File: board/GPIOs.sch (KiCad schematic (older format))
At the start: 3 parts

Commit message: Issue #1481 - GPIO sheet
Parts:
- gave numbers to parts that had none: 3
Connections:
- net labels added: DIFFCLK_A0N, DIFFCLK_A0P, DIFFCLK_A1N, DIFFCLK_A1P, DIFFCLK_B0N, DIFFCLK_B0P, DIFFCLK_B1N, DIFFCLK_B1P, DIFFCLK_XN, DIFFCLK_XP, DIFFIO_A0N, DIFFIO_A0P, DIFFIO_A1N, DIFFIO_A1P, DIFFIO_A2N, DIFFIO_A2P, DIFFIO_A3N, DIFFIO_A3P, DIFFIO_A4N, DIFFIO_A4P, DIFFIO_A5N, DIFFIO_A5P, DIFFIO_A6N, DIFFIO_A6P, DIFFIO_B0P, DIFFIO_B1N, DIFFIO_B1P, DIFFIO_B2N, DIFFIO_B2P, DIFFIO_B3N, DIFFIO_B3P, DIFFIO_B4N, DIFFIO_B4P, DIFFIO_B5N, DIFFIO_B5P, DIFFIO_B6N, DIFFIO_B6P, DIFFIO_XN, DIFFIO_XP, DIFFIO_YN, DIFFIO_YP, DIFFIO_ZN, DIFFIO_ZP, GPIO0, GPIO1, GPIO10, GPIO11, GPIO12, GPIO13, GPIO14, GPIO15, GPIO2, GPIO3, GPIO4, GPIO5, GPIO6, GPIO7, GPIO8, GPIO9, GPIO[0..15], PCIE_RESET, SMCLK, SMDATA, VCC3V3, ~RST
- net labels removed: GPIOA0, GPIOA1, GPIOA10, GPIOA11, GPIOA12, GPIOA13, GPIOA14, GPIOA15, GPIOA16, GPIOA17, GPIOA18, GPIOA19, GPIOA2, GPIOA20, GPIOA21, GPIOA22, GPIOA23, GPIOA24, GPIOA25, GPIOA26, GPIOA27, GPIOA28, GPIOA29, GPIOA3, GPIOA30, GPIOA31, GPIOA32, GPIOA33, GPIOA34, GPIOA35, GPIOA36, GPIOA37, GPIOA38, GPIOA39, GPIOA4, GPIOA40, GPIOA41, GPIOA42, GPIOA43, GPIOA44, GPIOA45, GPIOA46, GPIOA47, GPIOA48, GPIOA49, GPIOA5, GPIOA50, GPIOA51, GPIOA52, GPIOA53, GPIOA54, GPIOA6, GPIOA7, GPIOA8, GPIOA9, GPIOB0, GPIOB1, GPIOB10, GPIOB11, GPIOB12, GPIOB13, GPIOB14, GPIOB15, GPIOB16, GPIOB17, GPIOB18, GPIOB19, GPIOB2, GPIOB20, GPIOB21, GPIOB22, GPIOB23, GPIOB24, GPIOB25, GPIOB26, GPIOB27, GPIOB28, GPIOB29, GPIOB3, GPIOB30, GPIOB31, GPIOB32, GPIOB33, GPIOB34, GPIOB35, GPIOB36, GPIOB37, GPIOB38, GPIOB39, GPIOB4, GPIOB40, GPIOB41, GPIOB42, GPIOB43, GPIOB44, GPIOB45, GPIOB46, GPIOB47, GPIOB48, GPIOB49, GPIOB5, GPIOB50, GPIOB51, GPIOB52, GPIOB53, GPIOB6, GPIOB7, GPIOB8, GPIOB9
- wire segments 102 -> 131
- no-connect marks 5 -> 0

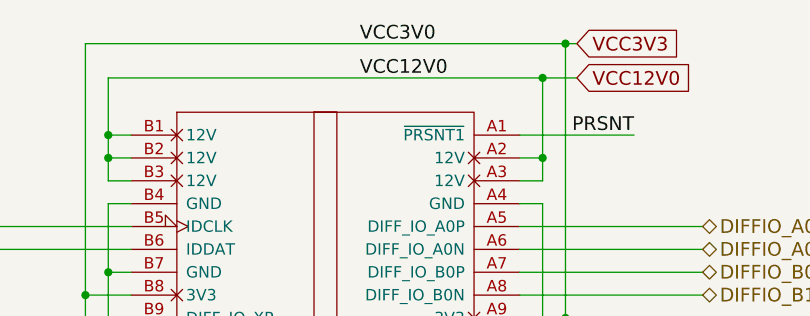
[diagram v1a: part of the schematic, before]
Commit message: Issue #1481 - CYPRESS-FPGA CONNECTIONS ADDED
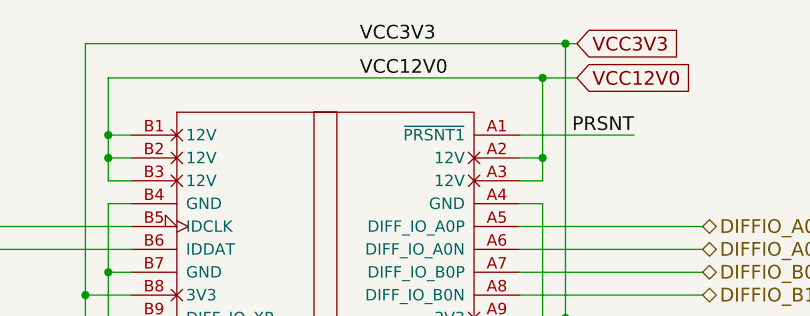
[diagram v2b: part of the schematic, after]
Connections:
- net VCC3V3: no longer P14.11, P14.12, P15.11, P15.12
- new net VCC3V0: P14.11, P14.12, P15.11, P15.12
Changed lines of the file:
@@
 $Descr A4 11693 8268
 encoding utf-8
-Sheet 12 12
+Sheet 10 12
 Title "HDMI2USB"
-Date "20 feb 2015"
+Date "24 feb 2015"
 Rev "Rev2"
 Comp ""
@@
 $EndComp
 $Comp
-L GND #PWR46
+L GND #PWR042
 U 1 1 54E50EB2
 P 4500 7200
-F 0 "#PWR46" H 4500 7200 30  0001 C CNN
+F 0 "#PWR042" H 4500 7200 30  0001 C CNN
 F 1 "GND" H 4500 7130 30  0001 C CNN
 F 2 "" H 4500 7200 60  0000 C CNN
@@
 VCC12V0
 Text Label 4650 1050 0    60   ~ 0
-VCC3V0
+VCC3V3
 $Comp
 L CONN_6X2 P14

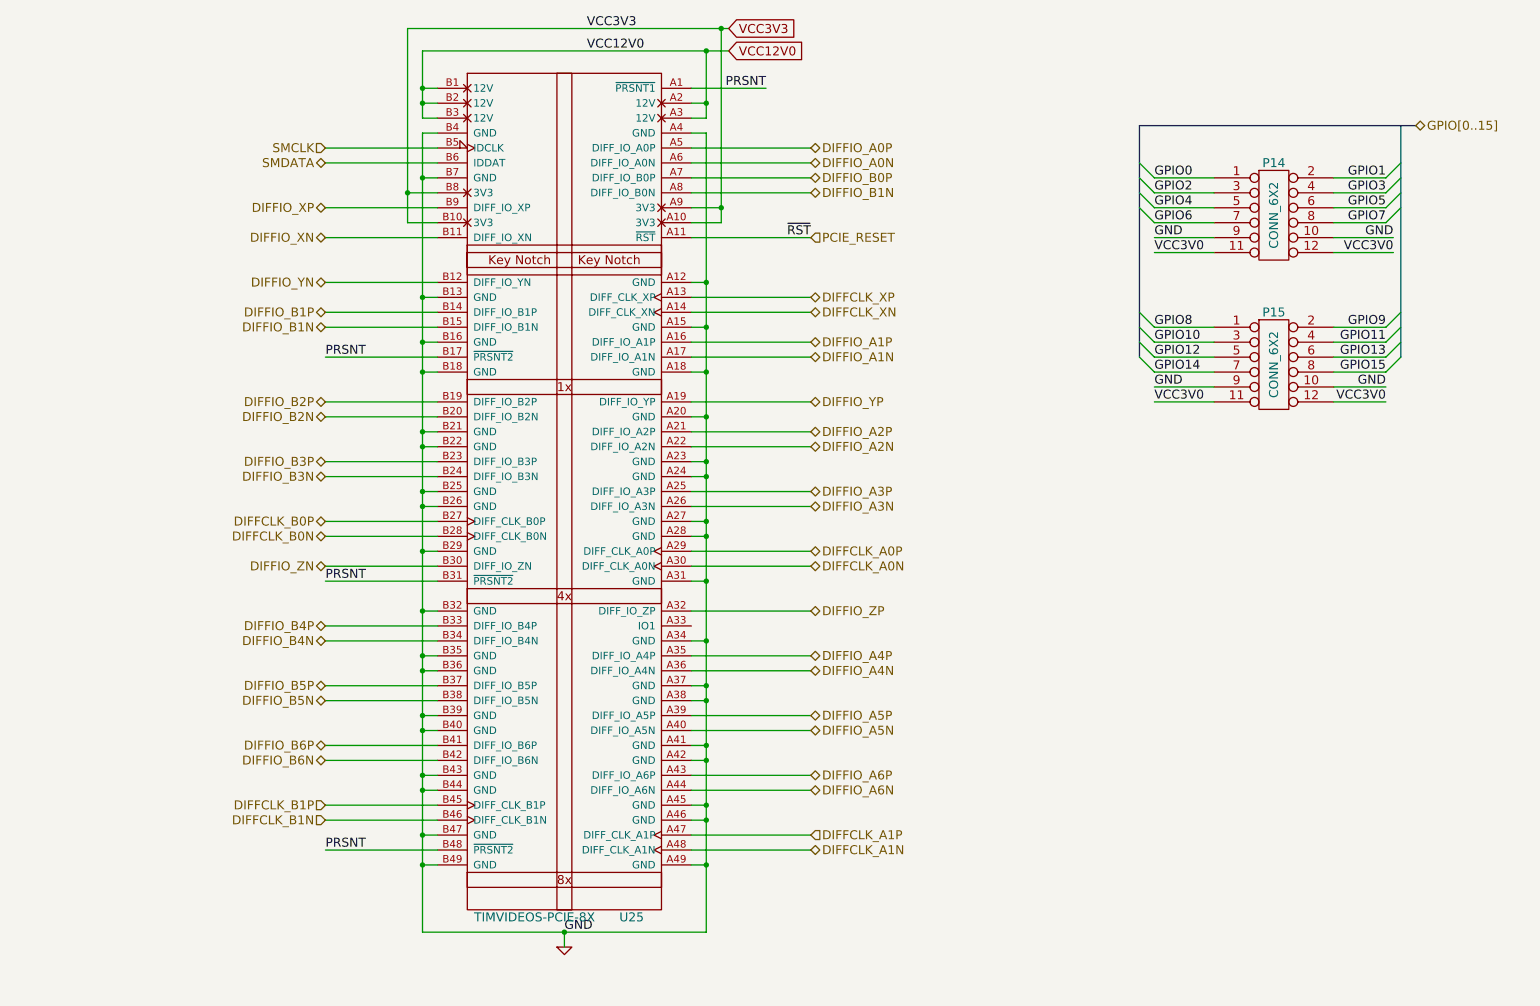
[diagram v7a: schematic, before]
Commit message: Issue #1680 - Bank 0 Ios
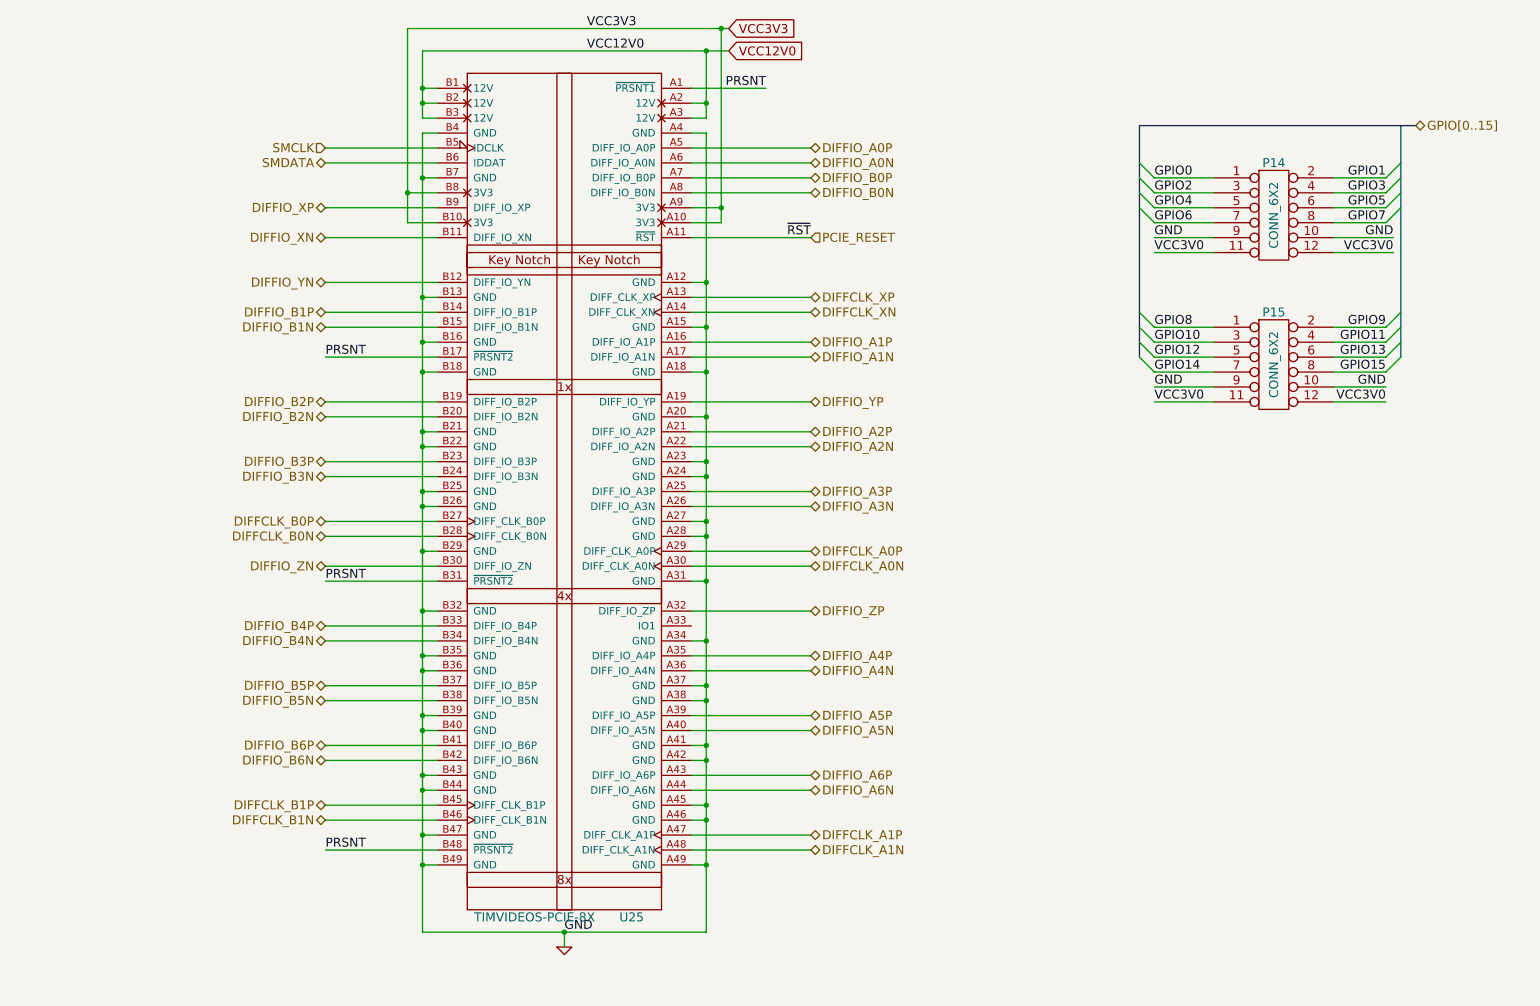
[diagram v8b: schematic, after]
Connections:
- net DIFFIO_B1N: no longer U25.A8 (DIFF_IO_B0N)
- new net DIFFIO_B0N: U25.A8 (DIFF_IO_B0N)
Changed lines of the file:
@@
 Sheet 10 12
 Title "HDMI2USB"
-Date "12 mar 2015"
+Date "23 mar 2015"
 Rev "Rev2"
 Comp ""
@@
 $EndComp
 $Comp
-L GND #PWR042
+L GND #PWR040
 U 1 1 54E50EB2
 P 4500 7200
-F 0 "#PWR042" H 4500 7200 30  0001 C CNN
+F 0 "#PWR040" H 4500 7200 30  0001 C CNN
 F 1 "GND" H 4500 7130 30  0001 C CNN
 F 2 "" H 4500 7200 60  0000 C CNN
@@
 Text HLabel 2900 5950 0    60   BiDi ~ 0
 DIFFIO_B6N
-Text HLabel 2900 6350 0    60   Input ~ 0
+Text HLabel 2900 6350 0    60   BiDi ~ 0
 DIFFCLK_B1N
-Text HLabel 6150 6450 2    60   Input ~ 0
+Text HLabel 6150 6450 2    60   BiDi ~ 0
 DIFFCLK_A1P
 Text HLabel 6150 3150 2    60   BiDi ~ 0
@@
 Text HLabel 2900 5850 0    60   BiDi ~ 0
 DIFFIO_B6P
-Text HLabel 2900 6250 0    60   Input ~ 0
+Text HLabel 2900 6250 0    60   BiDi ~ 0
 DIFFCLK_B1P
 Text Label 2900 3250 0    60   ~ 0
@@
 DIFFIO_A0P
 Text HLabel 6150 2150 2    60   BiDi ~ 0
-DIFFIO_B1N
+DIFFIO_B0N
 Text HLabel 6150 2050 2    60   BiDi ~ 0
 DIFFIO_B0P
